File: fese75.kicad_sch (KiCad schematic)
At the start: 180 parts, among them J1 MX-NoLED, K1 MX-NoLED, M1 MX-NoLED, P1 MX-NoLED, Q1 MX-NoLED, SW1 RotaryEncoder_Switch, T1 MX-NoLED, U1 MX-NoLED, U2 ATmega32U4-A, X1 MX-NoLED, Y1 MX-NoLED, Y2 Crystal_GND24_Small

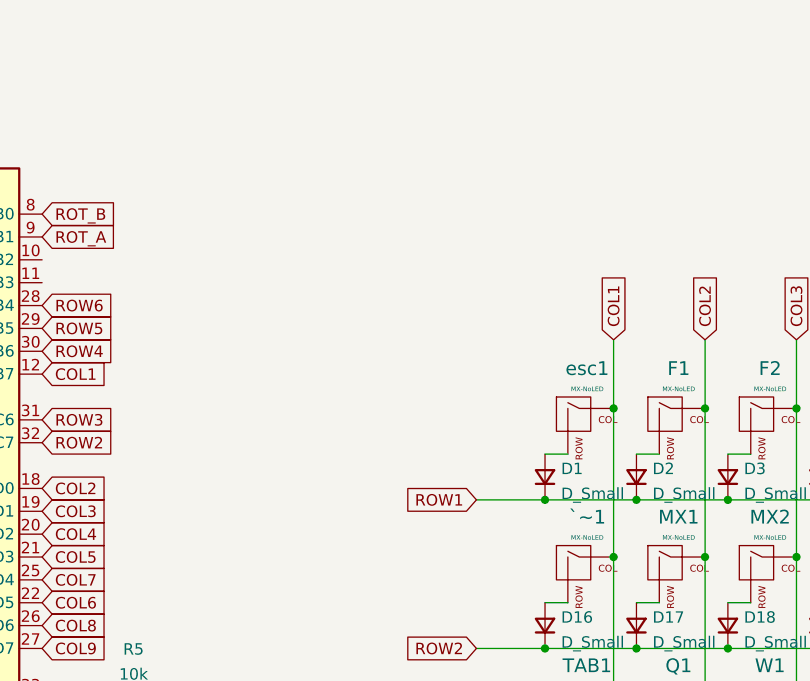
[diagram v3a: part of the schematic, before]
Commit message: fix some missing footprint
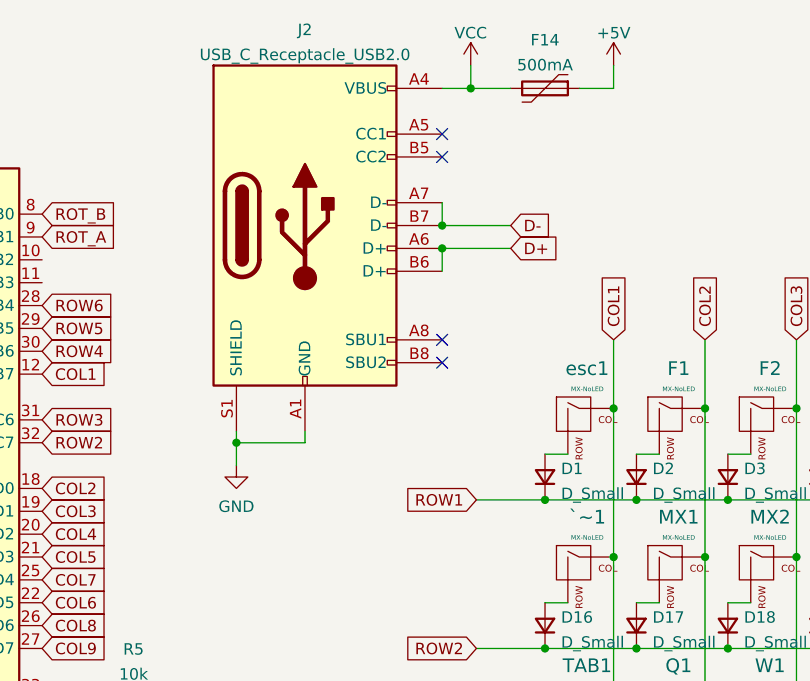
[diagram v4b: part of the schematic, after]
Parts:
- added F14: 500mA, symbol Device:Polyfuse
- added J2: USB_C_Receptacle_USB2.0, symbol Connector:USB_C_Receptacle_USB2.0
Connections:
- net +5V: now also F14.1
- net D+: now also J2.A6 (D+), J2.B6 (D+)
- net D-: now also J2.A7 (D-), J2.B7 (D-)
- net GND: now also J2.A1 (GND), J2.A12 (GND), J2.B1 (GND), J2.B12 (GND), J2.S1 (SHIELD)
- new net VCC: F14.2, J2.A4 (VBUS), J2.A9 (VBUS), J2.B4 (VBUS), J2.B9 (VBUS)
- no-connect marks 0 -> 4

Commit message: add type c and expand power
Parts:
- F14: footprint (none) -> Fuse:Fuse_1206_3216Metric
- J2: footprint (none) -> Connector_USB:USB_C_Receptacle_GCT_USB4085
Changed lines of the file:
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@@
     (property "Reference" "J2" (id 0) (at 96.52 11.2735 0))
     (property "Value" "USB_C_Receptacle_USB2.0" (id 1) (at 96.52 14.0486 0))
-    (property "Footprint" "" (id 2) (at 100.33 33.02 0)
+    (property "Footprint" "Connector_USB:USB_C_Receptacle_GCT_USB4085" (id 2) (at 100.33 33.02 0)
       (effects (font (size 1.27 1.27)) hide)
     )
@@
     (property "Reference" "F14" (id 0) (at 123.19 12.4165 90))
     (property "Value" "500mA" (id 1) (at 123.19 15.1916 90))
-    (property "Footprint" "" (id 2) (at 118.11 19.05 0)
+    (property "Footprint" "Fuse:Fuse_1206_3216Metric" (id 2) (at 118.11 19.05 0)
       (effects (font (size 1.27 1.27)) (justify left) hide)
     )
@@
     )
     (path "/9d355f05-5de2-41b8-8918-f0e30beea5c9"
-      (reference "F14") (unit 1) (value "500mA") (footprint "")
+      (reference "F14") (unit 1) (value "500mA") (footprint "Fuse:Fuse_1206_3216Metric")
     )
     (path "/f0797637-5ddb-4d87-aca5-a167dac34763"
@@
     )
     (path "/494cbc16-922a-405e-a1c7-f8125ccdd187"
-      (reference "J2") (unit 1) (value "USB_C_Receptacle_USB2.0") (footprint "")
+      (reference "J2") (unit 1) (value "USB_C_Receptacle_USB2.0") (footprint "Connector_USB:USB_C_Receptacle_GCT_USB4085")
     )
     (path "/fc996259-2a6c-4dd6-92ec-81d86507281b"

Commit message: fix2
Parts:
- added TP1: RESET, TestPoint:TestPoint_THTPad_1.0x1.0mm_Drill0.5mm, symbol Connector:TestPoint
- added TP2: GND, TestPoint:TestPoint_THTPad_D1.0mm_Drill0.5mm, symbol Connector:TestPoint
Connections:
- net GND: now also TP2.1
- net at R2.2, U2.13 (~{RESET}): now also TP1.1
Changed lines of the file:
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@@
     (pin "2")
   )
+  (symbol (lib_id "Connector:TestPoint") (at 29.21 31.75 90) (unit 1)
+    (in_bom yes) (on_board yes) (fields_autoplaced)
+    (property "Reference" "TP1" (id 0) (at 25.908 27.1485 90))
+    (property "Value" "RESET" (id 1) (at 25.908 29.9236 90))
+    (property "Footprint" "TestPoint:TestPoint_THTPad_1.0x1.0mm_Drill0.5mm" (id 2) (at 29.21 26.67 0)
+      (effects (font (size 1.27 1.27)) hide)
+    )
+    (property "Datasheet" "~" (id 3) (at 29.21 26.67 0)
+      (effects (font (size 1.27 1.27)) hide)
+    )
+    (pin "1")
+  )
   (symbol (lib_id "Device:D_Small") (at 214.63 93.98 90) (unit 1)
     (in_bom yes) (on_board yes) (fields_autoplaced)
@@
     (pin "2")
   )
+  (symbol (lib_id "Connector:TestPoint") (at 49.53 116.84 90) (unit 1)
+    (in_bom yes) (on_board yes) (fields_autoplaced)
+    (property "Reference" "TP2" (id 0) (at 46.228 112.2385 90))
+    (property "Value" "GND" (id 1) (at 46.228 115.0136 90))
+    (property "Footprint" "TestPoint:TestPoint_THTPad_D1.0mm_Drill0.5mm" (id 2) (at 49.53 111.76 0)
+      (effects (font (size 1.27 1.27)) hide)
+    )
+    (property "Datasheet" "~" (id 3) (at 49.53 111.76 0)
+      (effects (font (size 1.27 1.27)) hide)
+    )
+    (pin "1")
+  )
   (symbol (lib_id "MX_Alps_Hybrid:MX-NoLED") (at 147.32 54.61 0) (unit 1)
     (in_bom yes) (on_board yes) (fields_autoplaced)
@@
       (reference "TAB1") (unit 1) (value "MX-NoLED") (footprint "Switch_Keyboard_Kailh:SW_Hotswap_Kailh_1.50u")
     )
+    (path "/17d38d78-f73d-44f4-be6e-cfefc87955b2"
+      (reference "TP1") (unit 1) (value "RESET") (footprint "TestPoint:TestPoint_THTPad_1.0x1.0mm_Drill0.5mm")
+    )
+    (path "/cee219ad-8c82-484d-a421-38ba3038c9a2"
+      (reference "TP2") (unit 1) (value "GND") (footprint "TestPoint:TestPoint_THTPad_D1.0mm_Drill0.5mm")
+    )
     (path "/1de20f08-09dc-4bca-bd53-e579edc44b85"

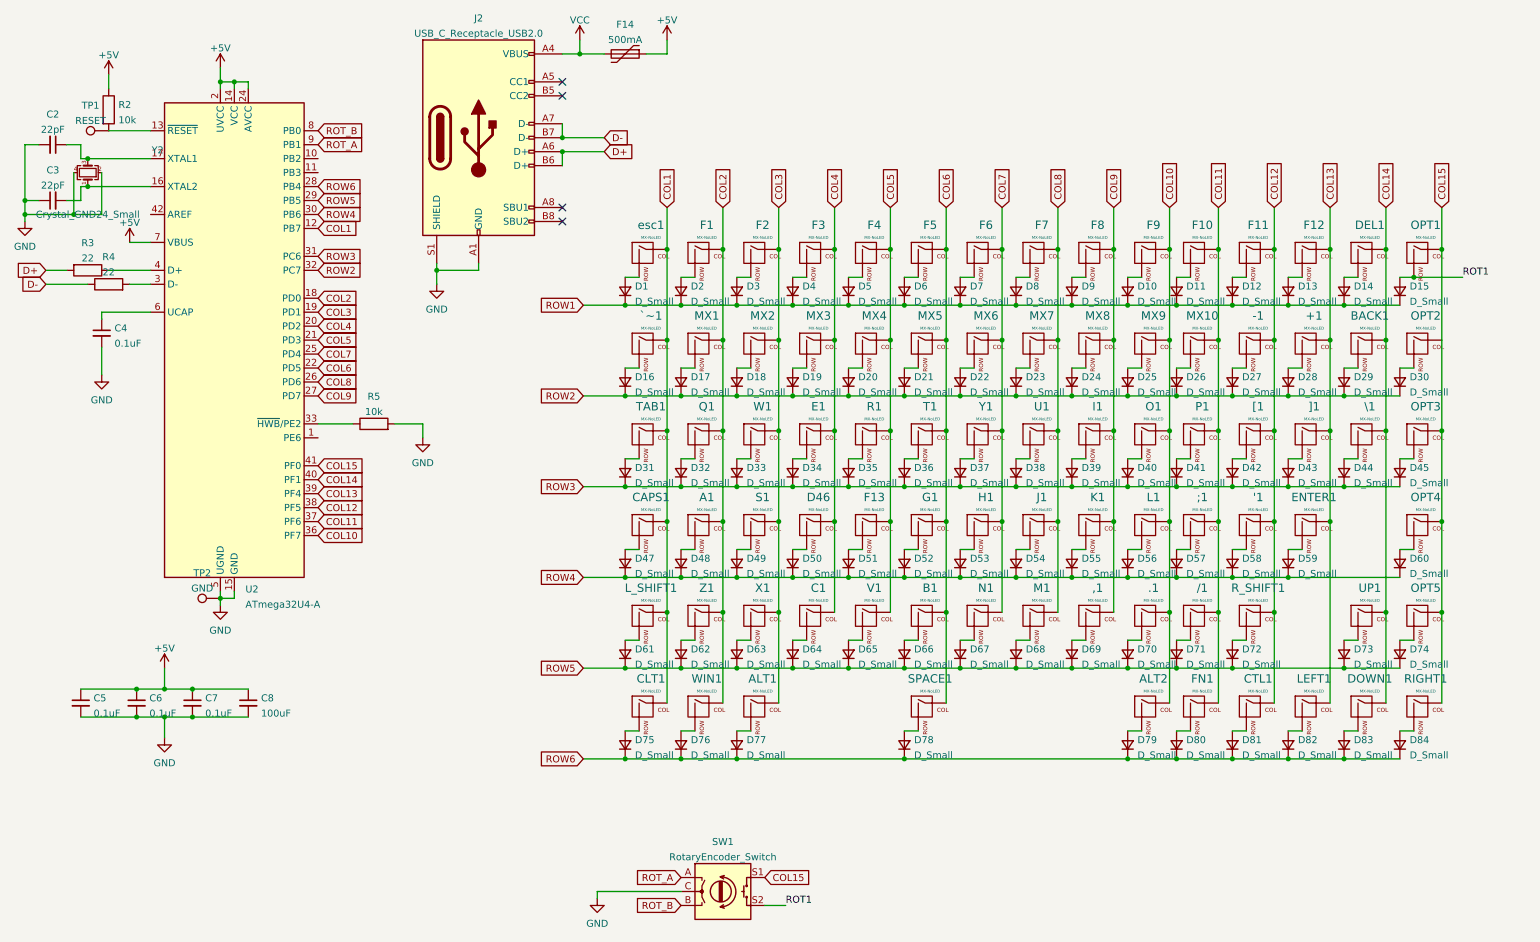
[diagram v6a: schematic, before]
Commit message: add testpoint
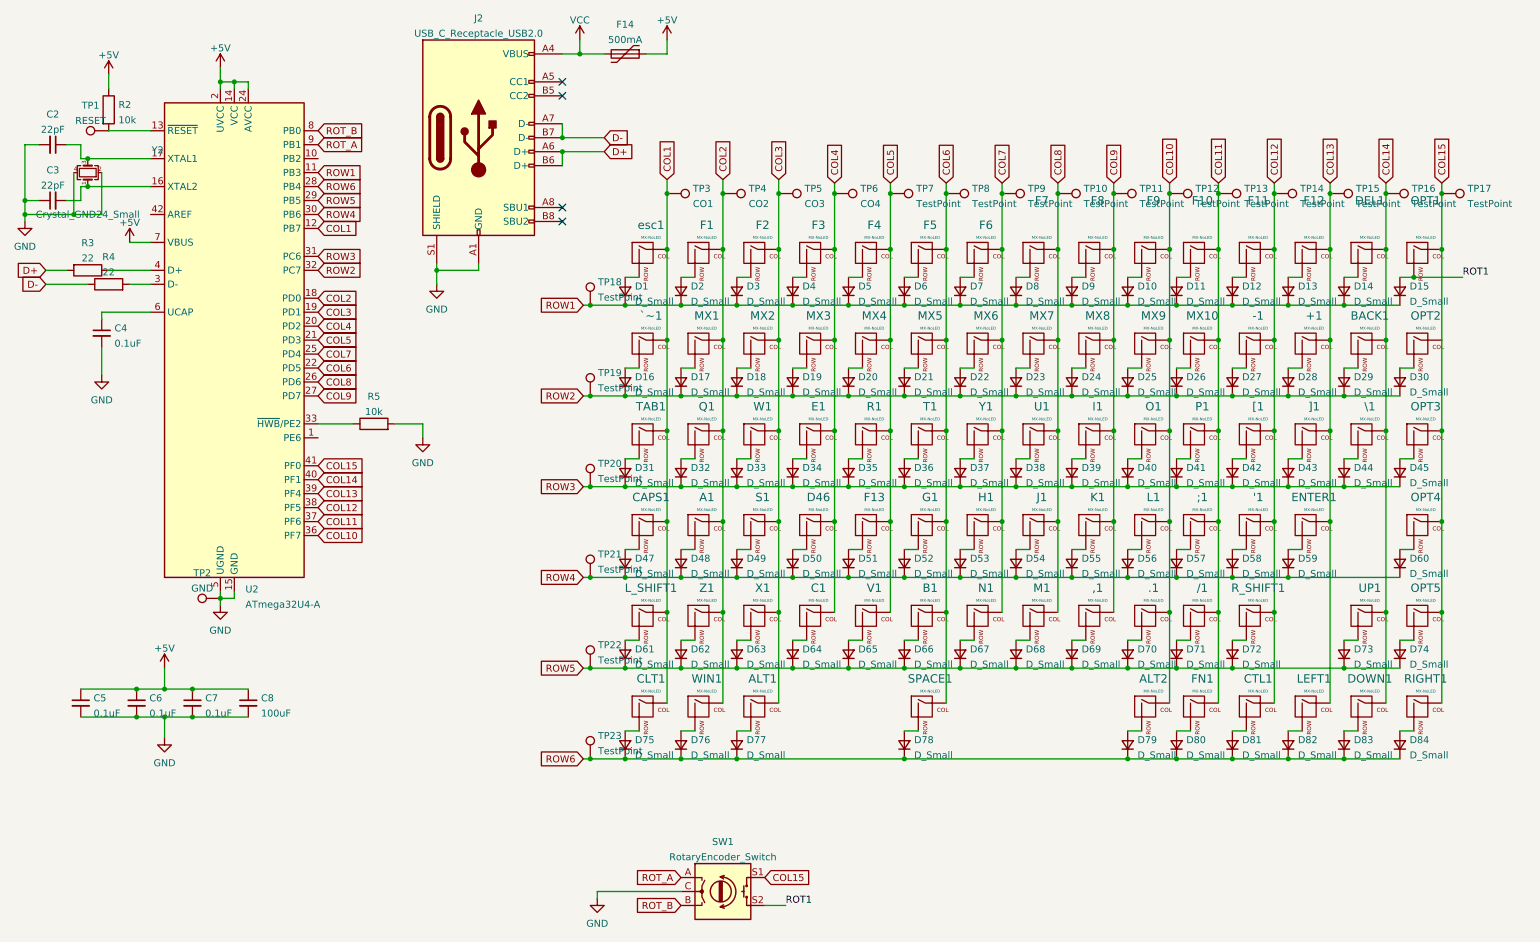
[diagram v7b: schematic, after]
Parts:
- added TP10, TP11, TP12, TP13, TP14, TP15, TP16, TP17, TP19, TP20, TP21, TP22, TP23, TP7, TP8, TP9: TestPoint, TestPoint:TestPoint_THTPad_D2.0mm_Drill1.0mm, symbol Connector:TestPoint
- added TP18: TestPoint, TestPoint:TestPoint_THTPad_2.0x2.0mm_Drill1.0mm, symbol Connector:TestPoint
- added TP3: CO1, TestPoint:TestPoint_THTPad_2.0x2.0mm_Drill1.0mm, symbol Connector:TestPoint
- added TP4: CO2, TestPoint:TestPoint_THTPad_D2.0mm_Drill1.0mm, symbol Connector:TestPoint
- added TP5: CO3, TestPoint:TestPoint_THTPad_D2.0mm_Drill1.0mm, symbol Connector:TestPoint
- added TP6: CO4, TestPoint:TestPoint_THTPad_D2.0mm_Drill1.0mm, symbol Connector:TestPoint
- TP1: footprint TestPoint:TestPoint_THTPad_1.0x1.0mm_Drill0.5mm -> TestPoint:TestPoint_THTPad_2.0x2.0mm_Drill1.0mm
- TP2: footprint TestPoint:TestPoint_THTPad_D1.0mm_Drill0.5mm -> TestPoint:TestPoint_THTPad_D2.0mm_Drill1.0mm
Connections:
- net COL1: now also TP3.1
- net COL10: now also TP12.1
- net COL11: now also TP13.1
- net COL12: now also TP14.1
- net COL13: now also TP15.1
- net COL14: now also TP16.1
- net COL15: now also TP17.1
- net COL2: now also TP4.1
- net COL3: now also TP5.1
- net COL4: now also TP6.1
- net COL5: now also TP7.1
- net COL6: now also TP8.1
- net COL7: now also TP9.1
- net COL8: now also TP10.1
- net COL9: now also TP11.1
- net ROW1: now also U2.11 (PB3), TP18.1
- net ROW2: now also TP19.1
- net ROW3: now also TP20.1
- net ROW4: now also TP21.1
- net ROW5: now also TP22.1
- net ROW6: now also TP23.1

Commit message: Finalize1
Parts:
- TP1: footprint TestPoint:TestPoint_THTPad_2.0x2.0mm_Drill1.0mm -> TestPoint:TestPoint_THTPad_D1.0mm_Drill0.5mm
- TP10: value TestPoint -> CO8
- TP11: value TestPoint -> CO9
- TP12: value TestPoint -> CO10
- TP13: value TestPoint -> CO11
- TP14: value TestPoint -> CO12
- TP15: value TestPoint -> CO13
- TP16: value TestPoint -> CO14
- TP17: value TestPoint -> CO15
- TP18: value TestPoint -> RO1
- TP19: value TestPoint -> RO2
- TP2: footprint TestPoint:TestPoint_THTPad_D2.0mm_Drill1.0mm -> TestPoint:TestPoint_THTPad_1.0x1.0mm_Drill0.5mm
- TP20: value TestPoint -> RO3
- TP21: value TestPoint -> RO4
- TP22: value TestPoint -> RO5
- TP23: value TestPoint -> RO6
- TP7: value TestPoint -> CO5
- TP8: value TestPoint -> CO6
- TP9: value TestPoint -> CO7
